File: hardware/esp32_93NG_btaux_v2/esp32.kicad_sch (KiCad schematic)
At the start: 12 parts, among them J1 SW_EXT, SW2 EN, SW3 BOOT, U8 ESP32-MINI-1

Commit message: Adjusted silkscreen labels to reduce clutter. Added GPIO header for external buttons or LEDs. Added second PCB faceplate, for the bottom-side of the assembly.
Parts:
- removed D1: LED_RGB, LED_SMD:LED_RGB_PLCC-6, symbol Device:LED_RGB
- removed R13, R14, R15: 1K, Resistor_SMD:R_0805_2012Metric, symbol Device:R_Small
- added J8: Conn_GPIO, Connector_PinHeader_2.54mm:PinHeader_2x04_P2.54mm_Vertical, symbol Connector_Generic:Conn_02x04_Odd_Even
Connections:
- net +3V3: now also J8.7 (Pin_7), J8.8 (Pin_8)
- net GND: now also J8.5 (Pin_5), J8.6 (Pin_6)
- net IO23: now reaches U8.31 (IO23)
- net IO23: now also J8.3 (Pin_3)
- net IO22: now reaches U8.33 (IO22)
- net IO22: now also J8.1 (Pin_1)
- net IO5: now reaches U8.29 (IO5)
- net IO5: now also J8.4 (Pin_4)
- net IO21: now reaches U8.34 (IO21)
- net IO21: now also J8.2 (Pin_2)
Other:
- note added: "SW_EXT is for wiring external switches to a more convenient location. Paired with a UART adaptor of suitable length, it should make in-car programming much easier."
- note added: "This is just a breakout to some GPIO pins, if external LEDs or buttons are desired."
- moved on the sheet: J1, R6, R7, R8, R9, SW2, SW3

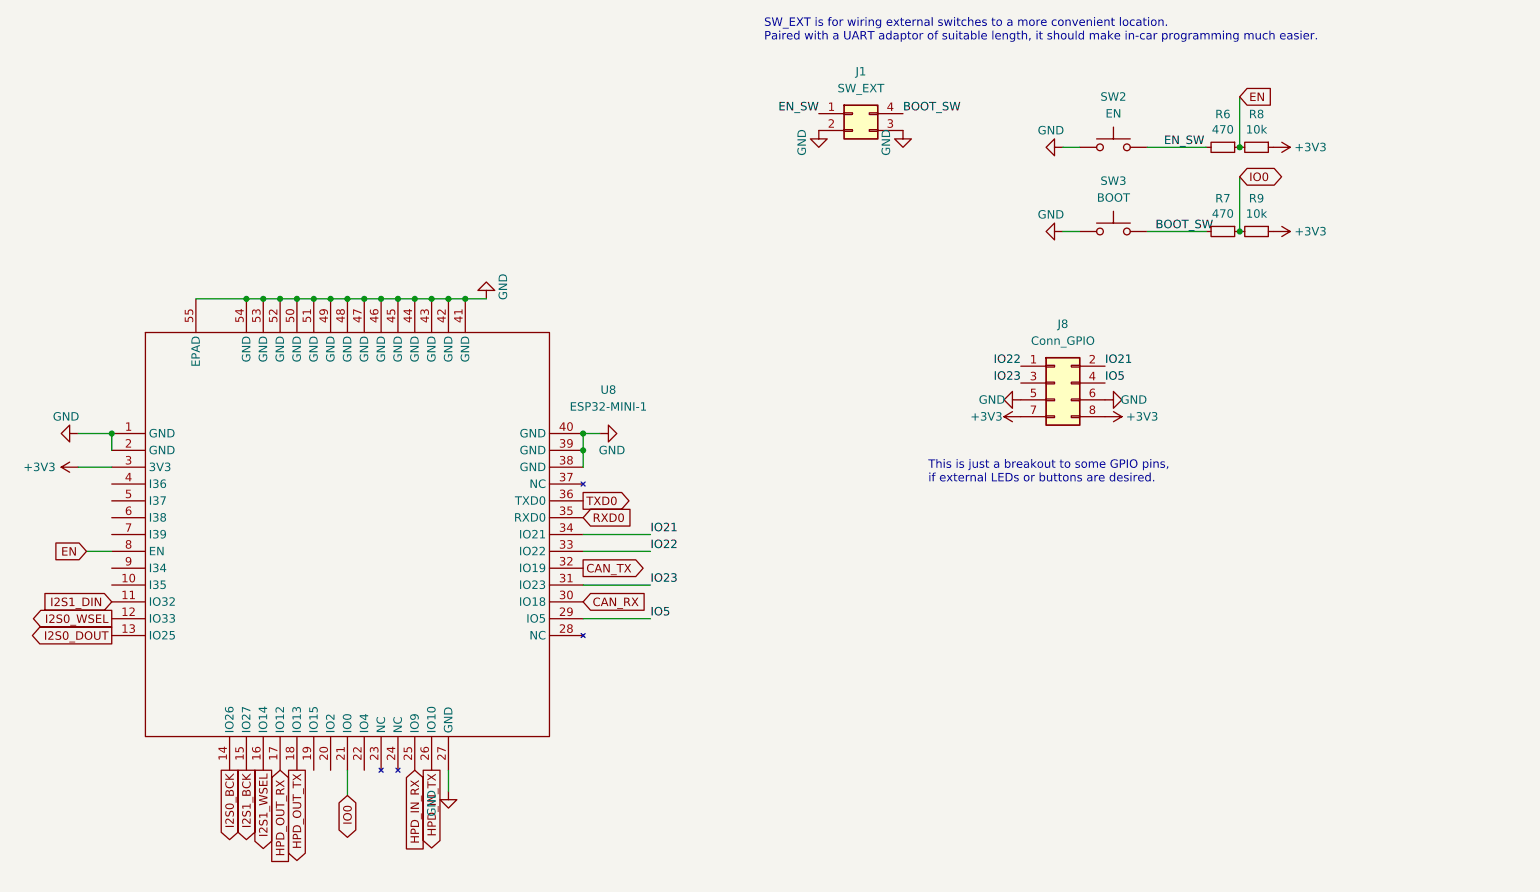
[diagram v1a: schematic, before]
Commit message: Started working on module-based V2 PCB, which is easier to build.
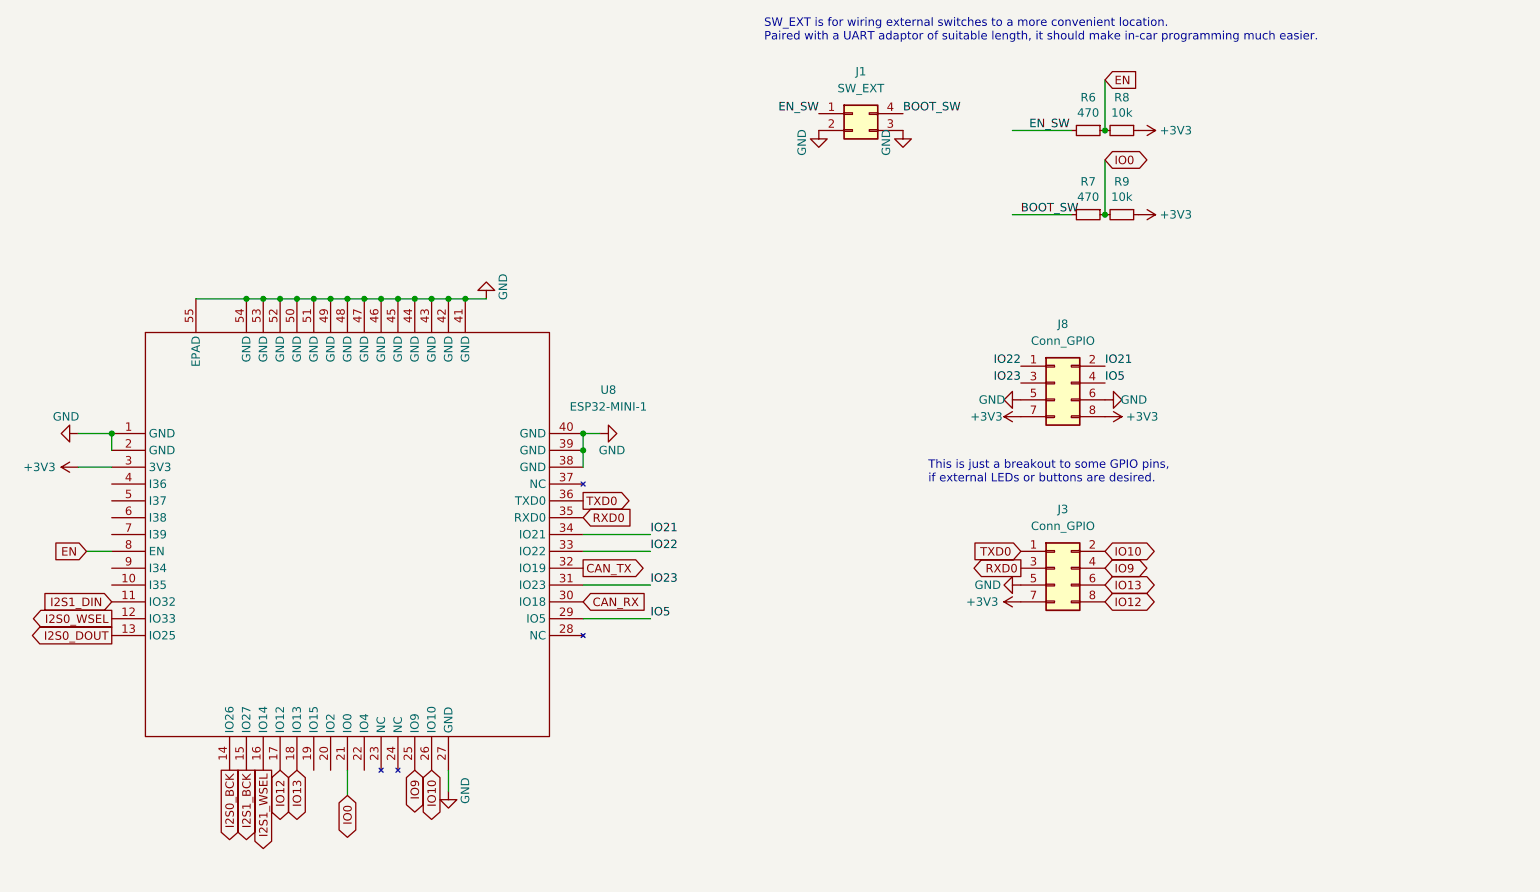
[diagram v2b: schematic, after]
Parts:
- removed SW2: EN, kicadlibrary:R-667834, symbol Switch:SW_Push
- removed SW3: BOOT, kicadlibrary:R-667834, symbol Switch:SW_Push
- added J3: Conn_GPIO, Connector_PinHeader_2.54mm:PinHeader_2x04_P2.54mm_Vertical, symbol Connector_Generic:Conn_02x04_Odd_Even
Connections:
- net +3V3: now also J3.7 (Pin_7)
- net GND: now also J3.5 (Pin_5)
- net RXD0: now also J3.3 (Pin_3)
- net TXD0: now also J3.1 (Pin_1)
- net HPD_IN_RX renamed IO9
- net IO9: now also J3.4 (Pin_4)
- net HPD_IN_TX renamed IO10
- net IO10: now also J3.2 (Pin_2)
- net HPD_OUT_RX renamed IO12
- net IO12: now also J3.8 (Pin_8)
- net HPD_OUT_TX renamed IO13
- net IO13: now also J3.6 (Pin_6)
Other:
- moved on the sheet: R6, R7, R8, R9
